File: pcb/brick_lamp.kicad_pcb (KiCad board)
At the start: 2 copper layers, 26.7 x 21 mm, 11 parts, among them J1 LED_24V_OUT, J2 24V_IN, J3 DEBUG, J4 DEBUG, Q1 CSD17302Q5A, U2 MCP1799x-330xxTT, U3 ATtiny85V-10S

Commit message: Cleanup schematics
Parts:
- moved J4 7.62 mm to (120.0, 90.2), turned to 0 degrees
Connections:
- J4 pad 2: PB4 -> PB5
- J4 pad 4: PB5 -> PB4
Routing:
- net PB5: track 5.94 -> 4.41 mm
- net PB4: track 4.41 -> 3.88 mm
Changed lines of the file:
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@@
 	(footprint "Connector_PinHeader_2.54mm:PinHeader_1x04_P2.54mm_Vertical"
 		(layer "F.Cu")
-		(at 120.015 97.79 180)
+		(at 120.015 90.17)
 		(descr "Through hole straight pin header, 1x04, 2.54mm pitch, single row")
 		(tags "Through hole pin header THT 1x04 2.54mm single row")
@@
 		(attr through_hole)
 		(fp_line
-			(start 1.38 1.27)
-			(end 1.38 9)
+			(start -1.38 -1.38)
+			(end 0 -1.38)
 			(stroke
 				(width 0.12)
@@
 		)
 		(fp_line
-			(start -1.38 9)
-			(end 1.38 9)
+			(start -1.38 0)
+			(end -1.38 -1.38)
 			(stroke
 				(width 0.12)
@@
 		(fp_line
 			(start -1.38 1.27)
-			(end 1.38 1.27)
+			(end -1.38 9)
 			(stroke
 				(width 0.12)
@@
 		(fp_line
 			(start -1.38 1.27)
-			(end -1.38 9)
+			(end 1.38 1.27)
 			(stroke
 				(width 0.12)
@@
 		)
 		(fp_line
-			(start -1.38 0)
-			(end -1.38 -1.38)
+			(start -1.38 9)
+			(end 1.38 9)
 			(stroke
 				(width 0.12)
@@
 		)
 		(fp_line
-			(start -1.38 -1.38)
-			(end 0 -1.38)
+			(start 1.38 1.27)
+			(end 1.38 9)
 			(stroke
 				(width 0.12)
@@
 		)
 		(fp_line
-			(start 1.77 9.39)
-			(end 1.77 -1.77)
+			(start -1.77 -1.77)
+			(end -1.77 9.39)
 			(stroke
 				(width 0.05)
@@
 		)
 		(fp_line
-			(start 1.77 -1.77)
-			(end -1.77 -1.77)
+			(start -1.77 9.39)
+			(end 1.77 9.39)
 			(stroke
 				(width 0.05)
@@
 		)
 		(fp_line
-			(start -1.77 9.39)
-			(end 1.77 9.39)
+			(start 1.77 -1.77)
+			(end -1.77 -1.77)
 			(stroke
 				(width 0.05)
@@
 		)
 		(fp_line
-			(start -1.77 -1.77)
-			(end -1.77 9.39)
+			(start 1.77 9.39)
+			(end 1.77 -1.77)
 			(stroke
 				(width 0.05)
@@
 		)
 		(fp_line
-			(start 1.27 8.89)
-			(end -1.27 8.89)
+			(start -1.27 -0.635)
+			(end -0.635 -1.27)
 			(stroke
 				(width 0.1)
@@
 		)
 		(fp_line
-			(start 1.27 -1.27)
-			(end 1.27 8.89)
+			(start -1.27 8.89)
+			(end -1.27 -0.635)
 			(stroke
 				(width 0.1)
@@
 		)
 		(fp_line
-			(start -1.27 8.89)
-			(end -1.27 -0.635)
+			(start 1.27 -1.27)
+			(end 1.27 8.89)
 			(stroke
 				(width 0.1)
@@
 		)
 		(fp_line
-			(start -1.27 -0.635)
-			(end -0.635 -1.27)
+			(start 1.27 8.89)
+			(end -1.27 8.89)
 			(stroke
 				(width 0.1)
@@
 		)
 		(pad "1" thru_hole rect
-			(at 0 0 180)
+			(at 0 0)
 			(size 1.7 1.7)
 			(drill 1)
@@
 		)
 		(pad "2" thru_hole circle
-			(at 0 2.54 180)
+			(at 0 2.54)
 			(size 1.7 1.7)
 			(drill 1)
 			(layers "*.Cu" "*.Mask")
 			(remove_unused_layers no)
-			(net 8 "PB4")
+			(net 6 "PB5")
 			(pinfunction "Pin_2")
 			(pintype "passive")
 		)
 		(pad "3" thru_hole circle
-			(at 0 5.08 180)
+			(at 0 5.08)
 			(size 1.7 1.7)
 			(drill 1)
@@
 		)
 		(pad "4" thru_hole circle
-			(at 0 7.62 180)
+			(at 0 7.62)
 			(size 1.7 1.7)
 			(drill 1)
 			(layers "*.Cu" "*.Mask")
 			(remove_unused_layers no)
-			(net 6 "PB5")
+			(net 8 "PB4")
 			(pinfunction "Pin_4")
 			(pintype "passive")
@@
 	)
 	(gr_text "PB5"
-		(at 124.46 90.805 0)
+		(at 124.46 93.345 0)
 		(layer "B.SilkS")
 		(effects
@@
 	)
 	(gr_text "GND"
-		(at 124.46 98.425 0)
+		(at 124.46 90.805 0)
 		(layer "B.SilkS")
 		(effects
@@
 	)
 	(gr_text "PB4\n"
-		(at 124.46 95.885 0)
+		(at 124.46 98.425 0)
 		(layer "B.SilkS")
 		(effects
@@
 	)
 	(gr_text "PB3"
-		(at 124.46 93.345 0)
+		(at 124.46 95.885 0)
 		(layer "B.SilkS")
 		(effects
@@
 	)
 	(via
-		(at 118.11 92.71)
+		(at 118.11 94.2975)
 		(size 0.6)
 		(drill 0.3)
@@
 	)
 	(via
-		(at 121.285 86.995)
+		(at 120.015 87.63)
 		(size 0.6)
 		(drill 0.3)
@@
 	)
 	(via
-		(at 118.745 87.63)
+		(at 118.11 90.17)
 		(size 0.6)
 		(drill 0.3)
@@
 	)
 	(segment
-		(start 123.635 93.79)
-		(end 123.635 94.615)
+		(start 123.635 94.615)
+		(end 121.92 94.615)
 		(width 0.25)
 		(layer "F.Cu")
@@
 	)
 	(segment
-		(start 120.015 90.17)
-		(end 123.635 93.79)
+		(start 121.92 94.615)
+		(end 120.015 92.71)
 		(width 0.25)
 		(layer "F.Cu")
@@
 	)
 	(segment
-		(start 123.19 95.885)
-		(end 123.635 95.885)
-		(width 0.2)
-		(layer "F.Cu")
-		(net 7)
-	)
-	(segment
-		(start 120.015 92.71)
-		(end 123.19 95.885)
+		(start 120.65 95.885)
+		(end 120.015 95.25)
 		(width 0.25)
 		(layer "F.Cu")
@@
 		(width 0.2)
 		(layer "F.Cu")
-		(net 8)
+		(net 7)
 	)
 	(segment
-		(start 123.635 97.155)
-		(end 122.555 97.155)
+		(start 123.635 95.885)
+		(end 120.65 95.885)
+		(width 0.25)
+		(layer "F.Cu")
+		(net 7)
+	)
+	(segment
+		(start 120.65 97.155)
+		(end 120.015 97.79)
 		(width 0.25)
 		(layer "F.Cu")
@@
 	)
 	(segment
-		(start 122.555 97.155)
-		(end 120.65 95.25)
+		(start 123.635 97.155)
+		(end 120.65 97.155)
 		(width 0.25)
 		(layer "F.Cu")

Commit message: Add name of the board to silkscreen; improve current capacity
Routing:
- net 24V+: track 20.2 -> 22.4 mm
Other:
- board text added: "TINNY DIMMER V1"
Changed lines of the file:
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@@
 			(pinfunction "Pin_1")
 			(pintype "passive")
+			(thermal_bridge_angle 45)
 		)
 		(pad "2" thru_hole circle
@@
 			(pinfunction "Pin_2")
 			(pintype "passive")
+			(zone_connect 1)
+			(thermal_bridge_width 1.25)
 		)
 		(embedded_fonts no)
@@
 			(pintype "passive")
 			(solder_paste_margin -0.05)
+			(zone_connect 1)
+			(thermal_bridge_width 1.5)
 		)
 		(pad "2" smd roundrect
@@
 			(pintype "passive")
 			(solder_paste_margin -0.05)
+			(zone_connect 1)
+			(thermal_bridge_width 1.5)
 		)
 		(pad "3" smd roundrect
@@
 			(pintype "passive")
 			(solder_paste_margin -0.05)
+			(zone_connect 1)
+			(thermal_bridge_width 1.5)
 		)
 		(pad "4" smd roundrect
@@
 			(pinfunction "Pin_1")
 			(pintype "passive")
+			(teardrops
+				(best_length_ratio 0.5)
+				(max_length 1)
+				(best_width_ratio 1)
+				(max_width 5)
+				(curved_edges yes)
+				(filter_ratio 0.9)
+				(enabled no)
+				(allow_two_segments yes)
+				(prefer_zone_connections yes)
+			)
 		)
 		(pad "2" thru_hole circle
@@
 		)
 	)
+	(gr_text "TINNY DIMMER V1"
+		(at 130 81 0)
+		(layer "F.SilkS")
+		(effects
+			(font
+				(size 1 1.25)
+				(thickness 0.25)
+				(bold yes)
+			)
+			(justify bottom)
+		)
+	)
 	(gr_text "PB2"
 		(at 132.715 93.345 0)
@@
 	)
 	(via
-		(at 118.745 85.09)
+		(at 118.745 87.63)
 		(size 0.6)
 		(drill 0.3)
@@
 	)
 	(via
-		(at 125.73 89.535)
+		(at 128.272544 89.371245)
+		(size 0.6)
+		(drill 0.3)
+		(layers "F.Cu" "B.Cu")
+		(free yes)
+		(net 1)
+	)
+	(via
+		(at 125.73 92.71)
 		(size 0.6)
 		(drill 0.3)
@@
 	)
 	(via
-		(at 124.46 92.71)
+		(at 123.19 92.71)
 		(size 0.6)
 		(drill 0.3)
@@
 	)
 	(via
-		(at 142.24 89.535)
+		(at 127.635 86.995)
 		(size 0.6)
 		(drill 0.3)
@@
 	)
 	(via
-		(at 128.905 93.345)
+		(at 142.24 89.535)
 		(size 0.6)
 		(drill 0.3)
@@
 	)
 	(via
-		(at 132.08 81.28)
+		(at 128.27 93.345)
 		(size 0.6)
 		(drill 0.3)
@@
 	)
 	(via
-		(at 135.89 89.535)
+		(at 132.08 81.28)
 		(size 0.6)
 		(drill 0.3)
@@
 	)
 	(via
-		(at 135.89 95.25)
+		(at 135.89 94.615)
 		(size 0.6)
 		(drill 0.3)
@@
 	)
 	(via
-		(at 120.015 87.63)
+		(at 121.285 87.672277)
 		(size 0.6)
 		(drill 0.3)
@@
 	)
 	(via
-		(at 135.89 93.345)
+		(at 135.89 92.075)
 		(size 0.6)
 		(drill 0.3)
@@
 	)
 	(via
-		(at 131.445 85.09)
+		(at 132.08 85.09)
 		(size 0.6)
 		(drill 0.3)
@@
 	)
 	(via
-		(at 121.92 99.06)
+		(at 121.92 98.425)
 		(size 0.6)
 		(drill 0.3)
@@
 	)
 	(via
-		(at 128.905 85.09)
+		(at 128.27 85.09)
 		(size 0.6)
 		(drill 0.3)
@@
 	)
 	(via
-		(at 137.795 81.915)
-		(size 0.6)
-		(drill 0.3)
-		(layers "F.Cu" "B.Cu")
-		(free yes)
-		(net 1)
-	)
-	(via
-		(at 121.92 90.17)
+		(at 121.285 92.075)
 		(size 0.6)
 		(drill 0.3)
@@
 	)
 	(via
-		(at 134.62 88.265)
+		(at 133.35 88.265)
 		(size 0.6)
 		(drill 0.3)
@@
 	)
 	(via
-		(at 135.89 91.44)
+		(at 138.43 95.885)
 		(size 0.6)
 		(drill 0.3)
@@
 	)
 	(via
-		(at 128.27 88.9)
+		(at 124.46 84.455)
 		(size 0.6)
 		(drill 0.3)
@@
 	)
 	(via
-		(at 118.11 90.17)
+		(at 118.11 90.805)
 		(size 0.6)
 		(drill 0.3)
@@
 	)
 	(via
-		(at 121.92 81.915)
+		(at 121.285 85.09)
 		(size 0.6)
 		(drill 0.3)
@@
 	)
 	(via
-		(at 121.285 84.455)
+		(at 118.745 84.455)
 		(size 0.6)
 		(drill 0.3)
@@
 	)
 	(via
-		(at 139.065 95.885)
+		(at 139.7 95.885)
 		(size 0.6)
 		(drill 0.3)
@@
 	)
 	(via
-		(at 121.92 97.79)
+		(at 135.89 99.06)
 		(size 0.6)
 		(drill 0.3)
@@
 	)
 	(segment
-		(start 138.88 90.62)
-		(end 133.985 85.725)
-		(width 0.75)
+		(start 138.245 90.62)
+		(end 133.985 86.36)
+		(width 2.2)
 		(layer "F.Cu")
 		(net 3)
@@
 	)
 	(segment
-		(start 122.555 85.09)
-		(end 123.19 84.455)
+		(start 133.985 86.36)
+		(end 133.985 85.725)
+		(width 2.2)
+		(layer "F.Cu")
+		(net 3)
+	)
+	(segment
+		(start 138.88 90.62)
+		(end 138.245 90.62)
+		(width 2.2)
+		(layer "F.Cu")
+		(net 3)
+	)
+	(segment
+		(start 125.41 91.12)
+		(end 125.76 91.12)
 		(width 0.5)
 		(layer "F.Cu")
@@
 	(segment
 		(start 123.19 89.535)
-		(end 124.175 89.535)
+		(end 123.825 89.535)
 		(width 0.5)
 		(layer "F.Cu")
@@
 	)
 	(segment
-		(start 124.175 89.535)
-		(end 125.76 91.12)
+		(start 123.825 89.535)
+		(end 125.41 91.12)
 		(width 0.5)
 		(layer "F.Cu")
@@
 	)
 	(segment
-		(start 123.19 84.455)
-		(end 125.095 84.455)
+		(start 129.54 88.265)
+		(end 130.175 87.63)
 		(width 0.5)
 		(layer "F.Cu")
@@
 	)
 	(segment
-		(start 122.555 88.9)
-		(end 122.555 85.09)
+		(start 130.175 87.63)
+		(end 130.175 83.185)
 		(width 0.5)
 		(layer "F.Cu")
@@
 	)
 	(segment
-		(start 123.19 89.535)
-		(end 122.555 88.9)
+		(start 123.825 89.535)
+		(end 125.095 88.265)
+		(width 0.5)
+		(layer "F.Cu")
+		(net 4)
+	)
+	(segment
+		(start 125.095 88.265)
+		(end 129.54 88.265)
 		(width 0.5)
 		(layer "F.Cu")
@@
 	(segment
 		(start 126.365 83.185)
-		(end 133.985 83.185)
-		(width 0.75)
+		(end 130.175 83.185)
+		(width 2.2)
 		(layer "F.Cu")
 		(net 4)
 	)
 	(segment
-		(start 125.095 84.455)
-		(end 126.365 83.185)
-		(width 0.5)
+		(start 130.175 83.185)
+		(end 133.985 83.185)
+		(width 2.2)
 		(layer "F.Cu")
 		(net 4)

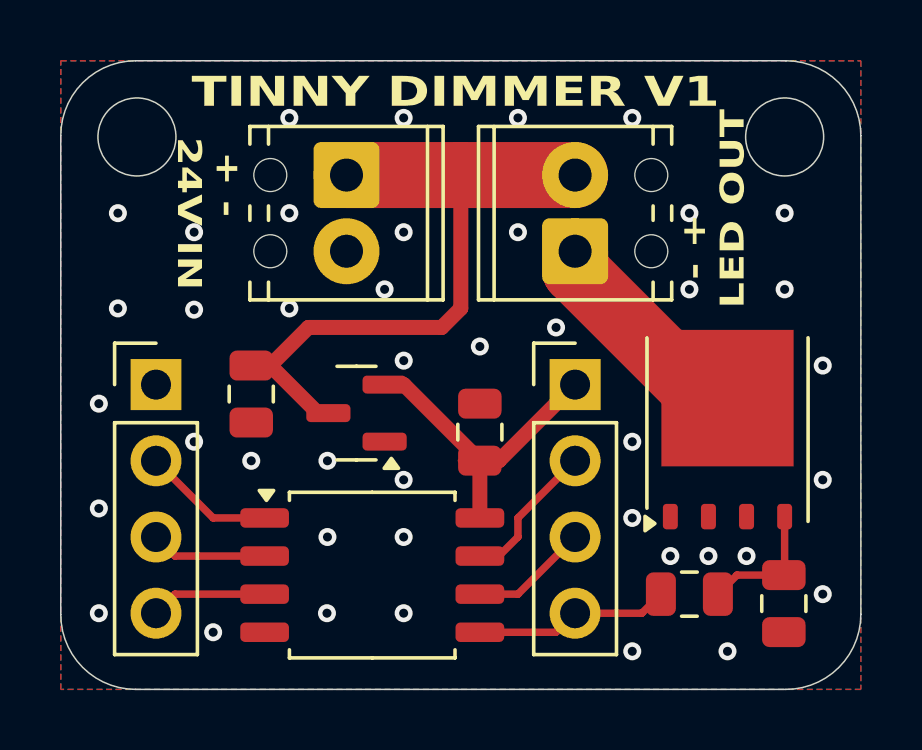
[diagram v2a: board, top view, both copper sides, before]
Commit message: Make the two pin headers breadboard compatible
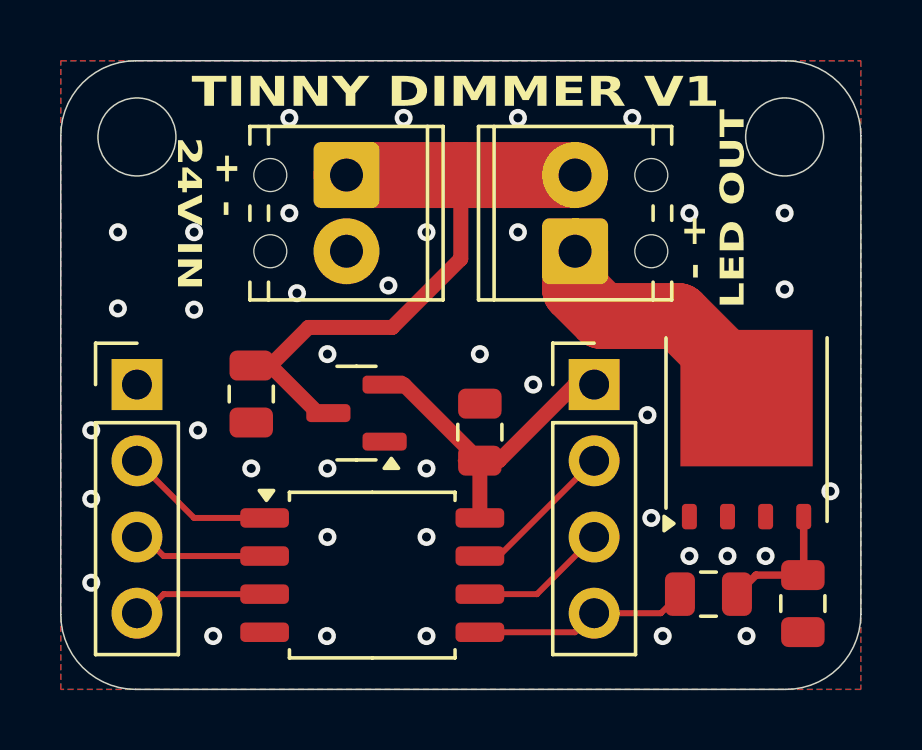
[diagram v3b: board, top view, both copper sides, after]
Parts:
- moved R2 0.64 mm to (138.4, 97.2)
- moved J4 0.64 mm to (119.4, 90.2)
- moved J3 0.63 mm to (134.6, 90.2)
- moved Q1 0.63 mm to (139.7, 91.7)
- moved R3 0.63 mm to (141.6, 97.5)
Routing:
- net Net-(J1-Pin_1): track 8.56 -> 9.57 mm
- net 24V+: track 22.4 -> 21.5 mm
- net PB4: track 3.88 -> 4.52 mm
- net PB5: track 4.41 -> 5.04 mm
- net PB1: track 3.96 -> 4.60 mm
- net MOSFET_GATE: track 4.58 -> 3.99 mm
- net GND: vias 42 -> 39

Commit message: Make it tiny not tinny
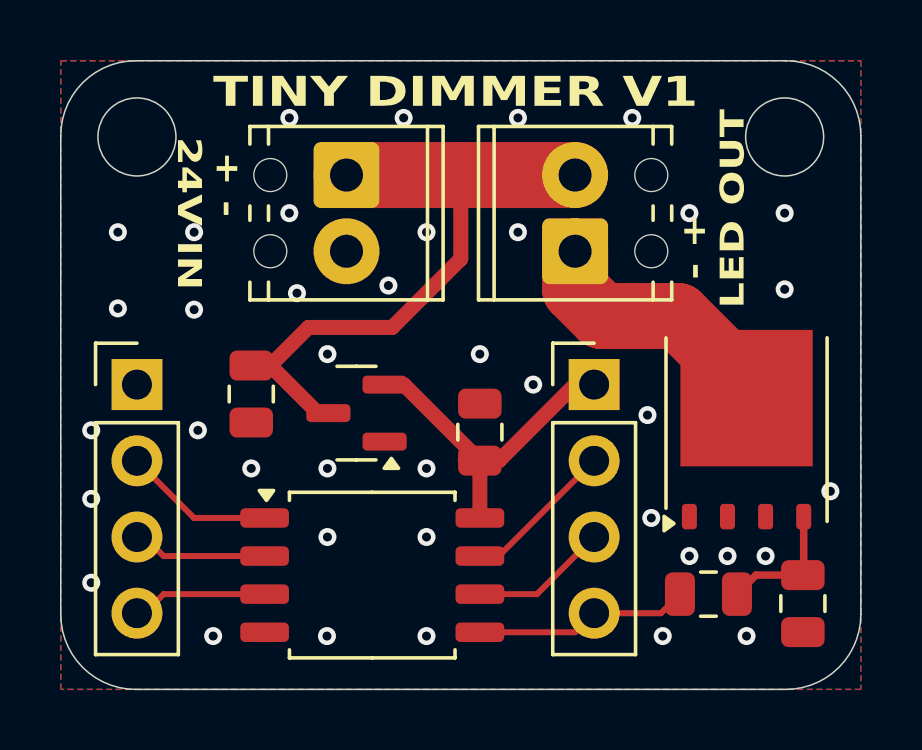
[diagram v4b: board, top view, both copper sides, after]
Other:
- board text added: "TINY DIMMER V1"
- board text removed: "TINNY DIMMER V1"
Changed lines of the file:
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@@
 		)
 	)
-	(gr_text "TINNY DIMMER V1"
+	(gr_text "TINY DIMMER V1"
 		(at 130 81 0)
 		(layer "F.SilkS")
